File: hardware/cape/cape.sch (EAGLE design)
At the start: 162 parts, among them IC1 AD8422BRMZ, IC10 DAC8562_DGS_10, IC11 CAT24C256WI-GT3, IC12 LM27762DSSR, IC13 BQ25504_RGT_16, IC14 SN74LV4T125PWR, IC15 LMP7701MF, IC16 TXB0304RUTR, IC2 OPA2388DGK8_L, IC3 AD8422BRMZ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

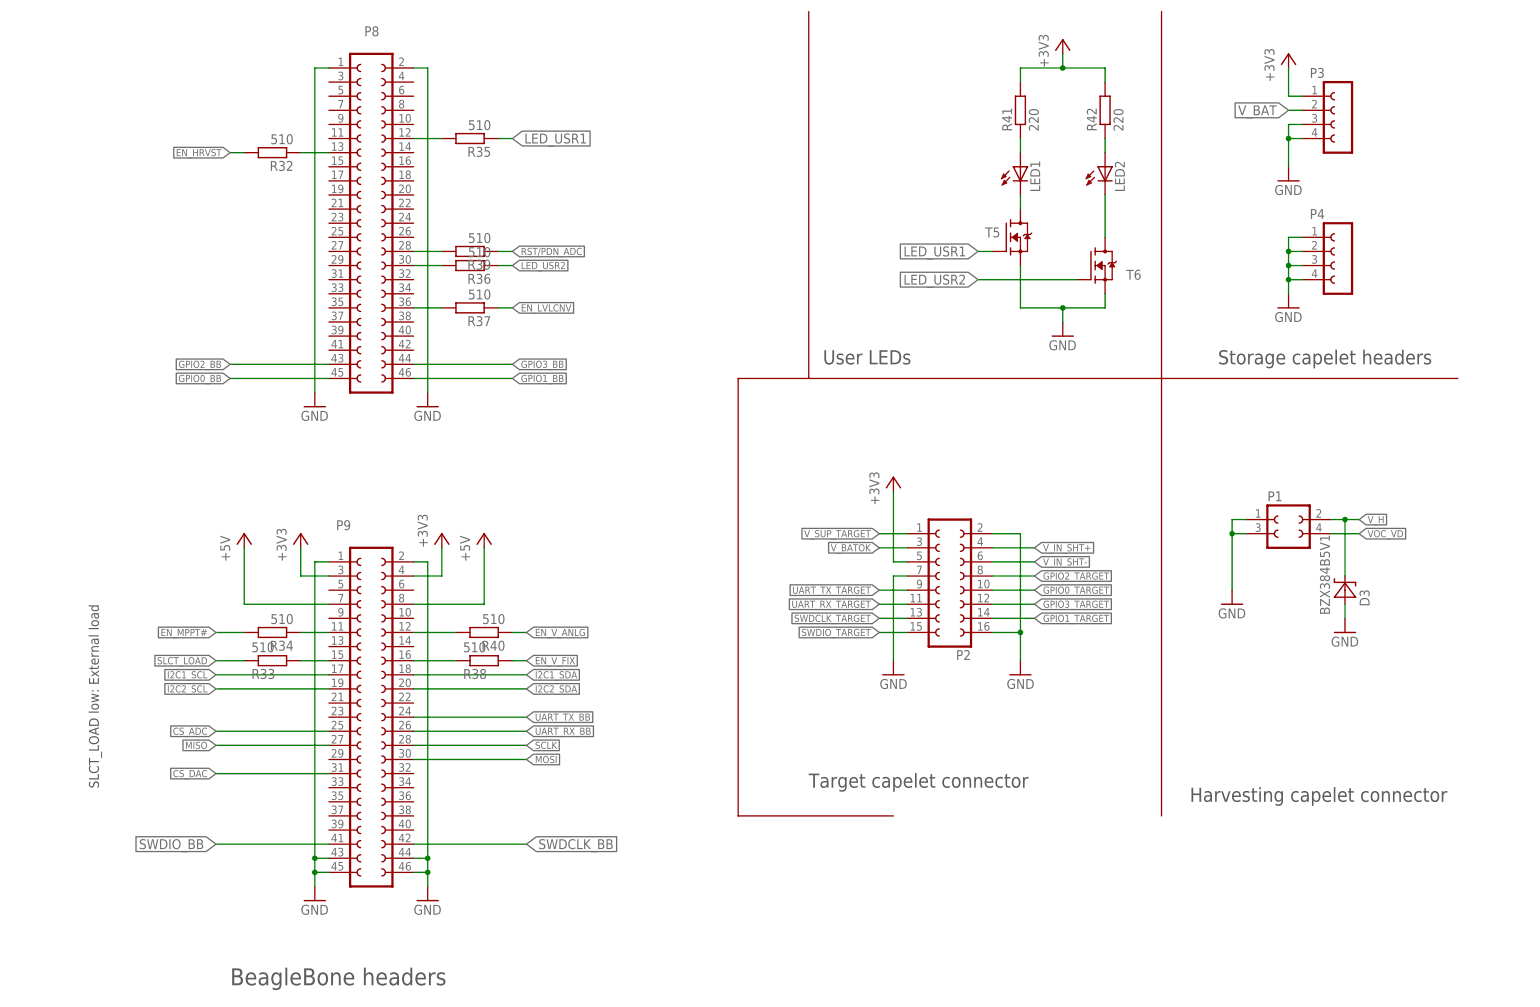
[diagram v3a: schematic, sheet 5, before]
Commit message: hardware: fancy frames for cape schematics
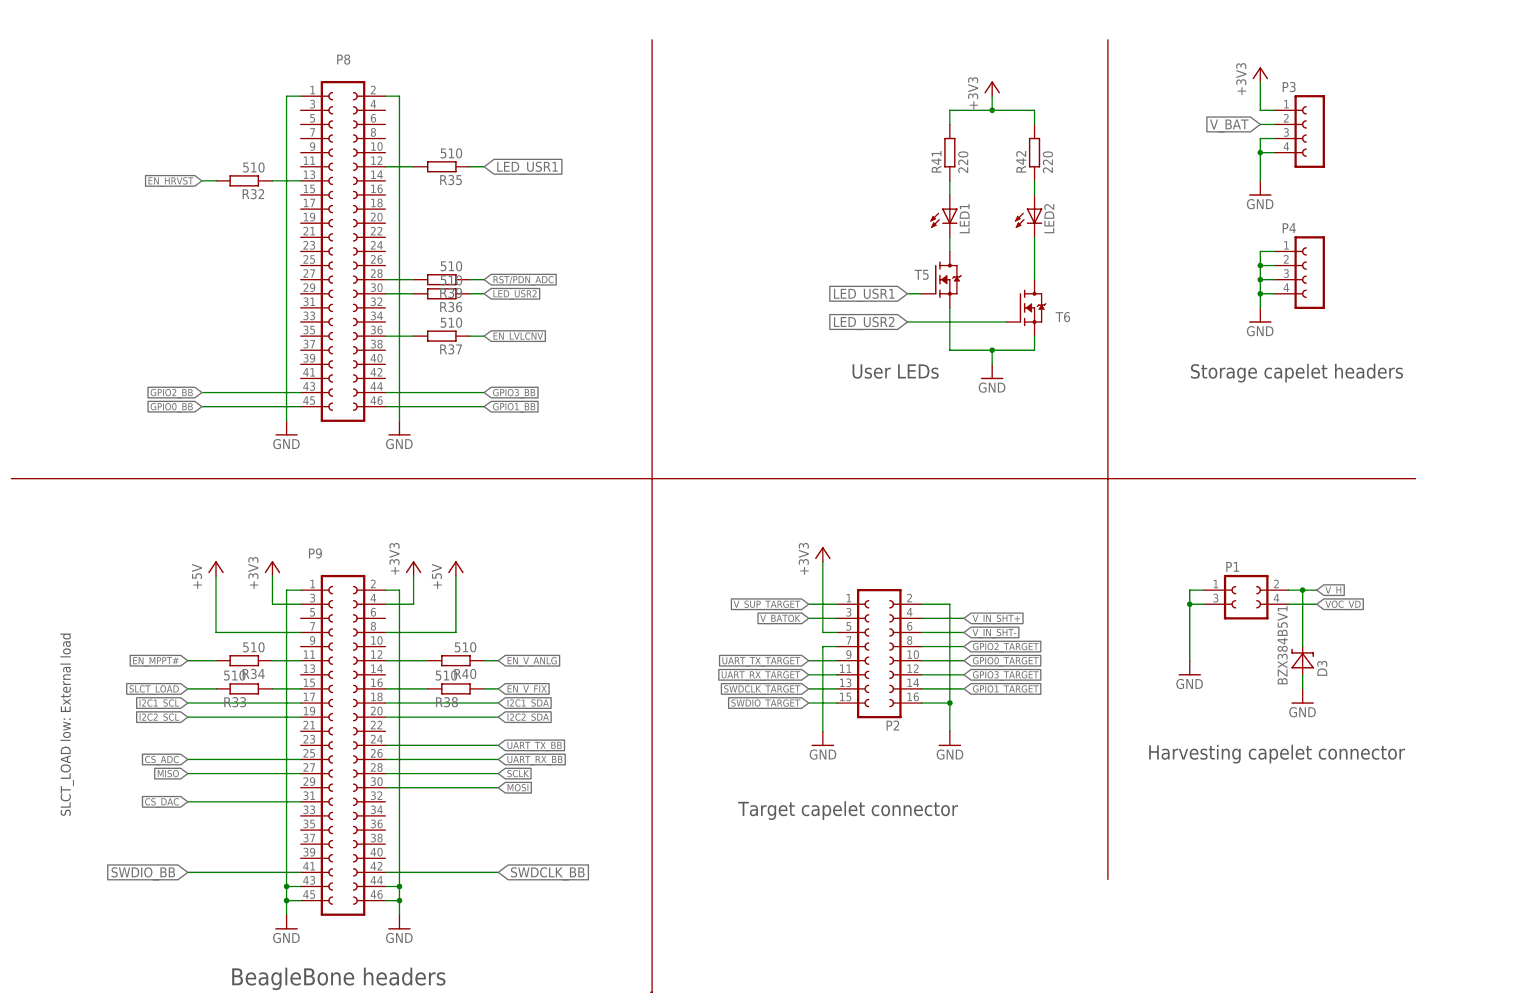
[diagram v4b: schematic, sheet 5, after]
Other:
- moved on the sheet: C1, C12, C13, C14, C15, C16, C17, C18, C19, C20, C21, C22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

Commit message: hardware: replaced LDO diode with switch connected to PRU+ARM. Added connector for illuminated button.
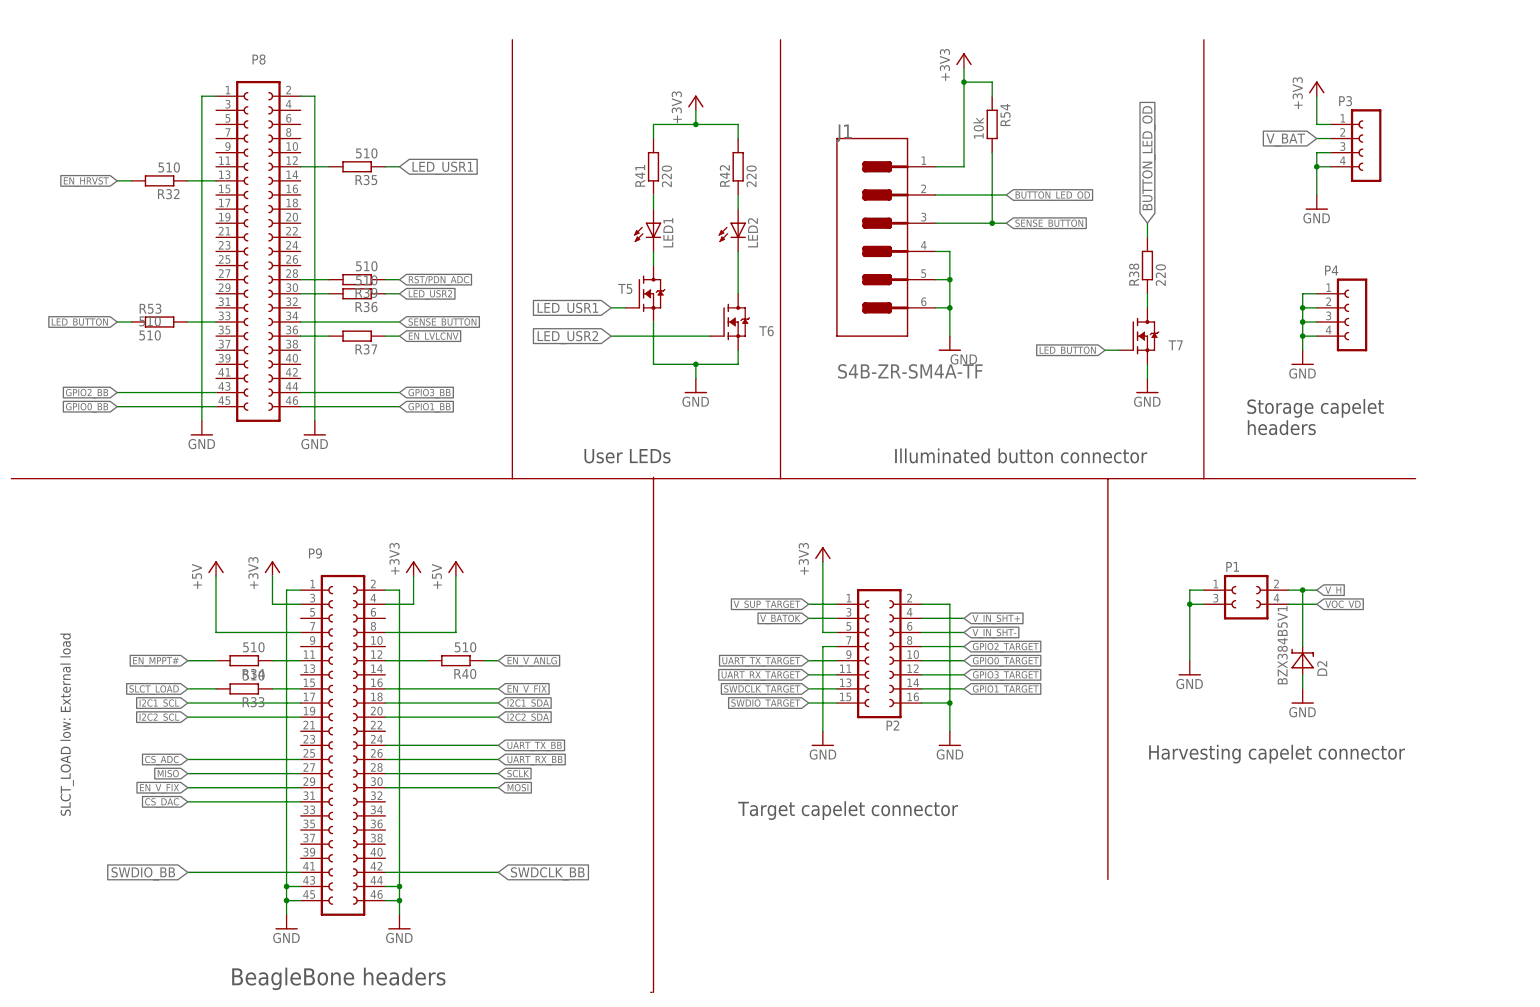
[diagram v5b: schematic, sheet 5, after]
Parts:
- removed D7: ACDBQC0130L-HF0402, shepherd:ACDBQC0130L-HF0402
- added C52: 1u, shepherd:C_SMD0603
- added C53: 0.1u, mylib:C_SMD0402
- added J1: JST_S4B-ZR-SM4A-TFJST_S4B-ZR-SM4A-TF_0_0, shepherd:JST_S4B-ZR-SM4A-TFJST_S4B-ZR-SM4A-TF_0_0
- added R53: 510, mylib:R_SMD0402
- added R54: 10k, mylib:R_SMD0402
- added S4: TMUX1101DCK, shepherd:TMUX1101DCK
- added T7: SI2374DSSOT23-VSHAY, mylib:SI2374DSSOT23-VSHAY
- D2: value BAT43WS-HE3SOD-323 -> BZX384B5V1; device mylib:BAT43WS-HE3SOD-323 -> mylib:BZX384B5V1
- D3: value BZX384B5V1 -> ACDBQC0130L-HF0402; device mylib:BZX384B5V1 -> shepherd:ACDBQC0130L-HF0402
- R38: value 510 -> 220; device mylib:R_SMD0402 -> mylib:R_SMD0603
- renumbered K1 to S3
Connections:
- new net BUTTON_LED_OD: J1.2, R38.2
- new net LED_BUTTON: R53.1, T7.G
- new net N$53: R38.1, T7.D
- new net SENSE_BUTTON: J1.3, P8.34, R54.2
- net +3V3: now also J1.1, R54.1
- net EN_V_FIX: now also P9.16, P9.29, S4.SEL; no longer IC8.EN, R38.2
- net GND: now also C52.2, C53.2, D2.A, J1.4, J1.MNT_1, J1.MNT_2, S4.GND, T7.S; no longer D3.A
- net GPIO0_BB: now also D5.C; no longer D7.C
- net GPIO1_BB: now also D3.C; no longer D5.C
- net N$14: now also R33.1; no longer R33.2
- net N$28: now also P8.33, R53.2; no longer P9.16, R38.1
- net N$47: now also D3.A; no longer D5.A
- net N$51: now also D5.A; no longer D7.A
- net N$7: now also C52.1, S4.D; no longer D2.A
- net SLCT_LOAD: now also R33.2; no longer R33.1
- net VDD: now also C53.1, IC8.EN, S4.VDD
- net V_H: now also D2.C; no longer D3.C
- net V_LD_SHT+: now also S4.S; no longer D2.C
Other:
- note added: "Illuminated button connector"
- moved on the sheet: C26, C27, C28, D5, IC7, IC8, LED1, LED2, P3, P4, P8, R22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
